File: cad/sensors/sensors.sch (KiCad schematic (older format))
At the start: 75 parts, among them J1 Conn_01x04, J2 Conn_01x04, J3 6P6C, J4 Conn_01x04, J5 Conn_01x04, J6 Conn_01x04, J7 Conn_01x02, U1 LMV324, U2 PCA9517A, U3 LMV331, U4 MC14040B, U5 MC14040B, U6 TCA9555DBR, U7 PCF8574

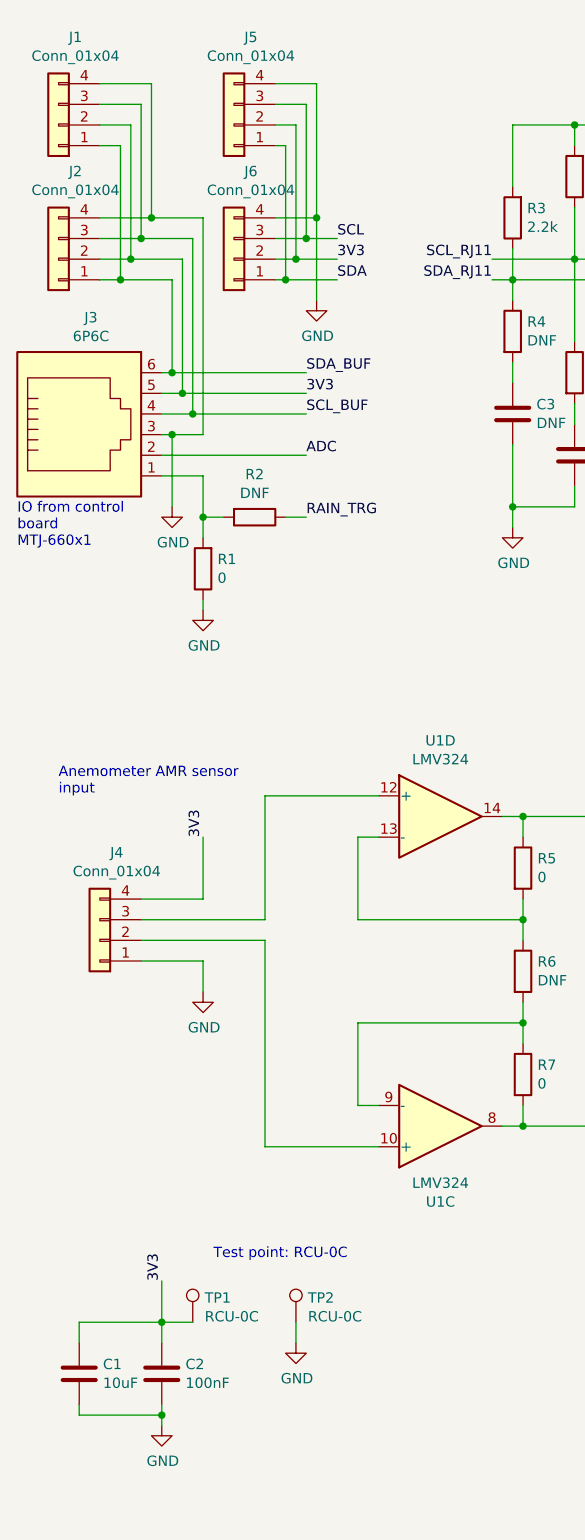
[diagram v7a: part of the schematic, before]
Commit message: Finished routing sensor breakout board. Need to draw power planes
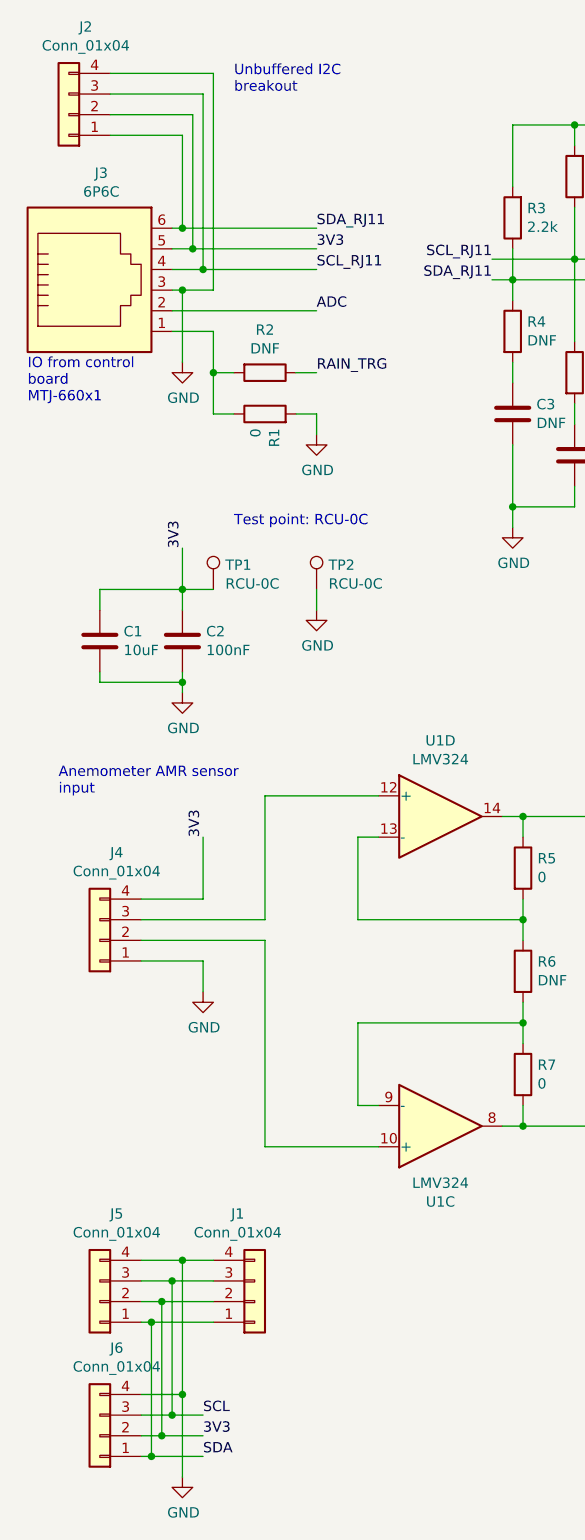
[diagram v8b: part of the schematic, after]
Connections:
- net GND: now also R1.2; no longer R1.1
- net SCL: now also J1.3 (Pin_3)
- net SCL_RJ11: now also J2.3 (Pin_3), J3.4
- net SDA: now also J1.1 (Pin_1)
- net SDA_RJ11: now also J2.1 (Pin_1), J3.6
- net at J3.1, R2.2: now also R1.1; no longer R1.2
- removed net SCL_BUF: J1.3 (Pin_3), J2.3 (Pin_3), J3.4
- removed net SDA_BUF: J1.1 (Pin_1), J2.1 (Pin_1), J3.6
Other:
- note added: "Unbuffered I2C \nbreakout"
- moved on the sheet: C1, C2, J1, J2, J3, J5, J6, R1, R2, TP1, TP2
